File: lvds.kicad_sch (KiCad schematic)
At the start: 19 parts, among them IC10 DS90LV048ATM_NOPB, IC8 DS90LV048ATM_NOPB, IC9 DS90LV048ATM_NOPB

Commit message: Lots of small changes
Some power and ground planes need to be looked at
All parts need to be reexamined before ordering
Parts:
- RLVDS10, RLVDS11, RLVDS2, RLVDS3, RLVDS4, RLVDS5, RLVDS6, RLVDS7, RLVDS8, RLVDS9: Mouser Part Number 71-CRCW0603100RFKEAH -> 667-ERJ-P03F1000V; Mouser Price/Stock https://www.mouser.com/ProductDetail/Vishay-Dale/CRCW060310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 -> https://www.mouser.com/ProductDetail/Panasonic/ERJ-P03F1000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; Power Rating 0.33W -> 0.2W

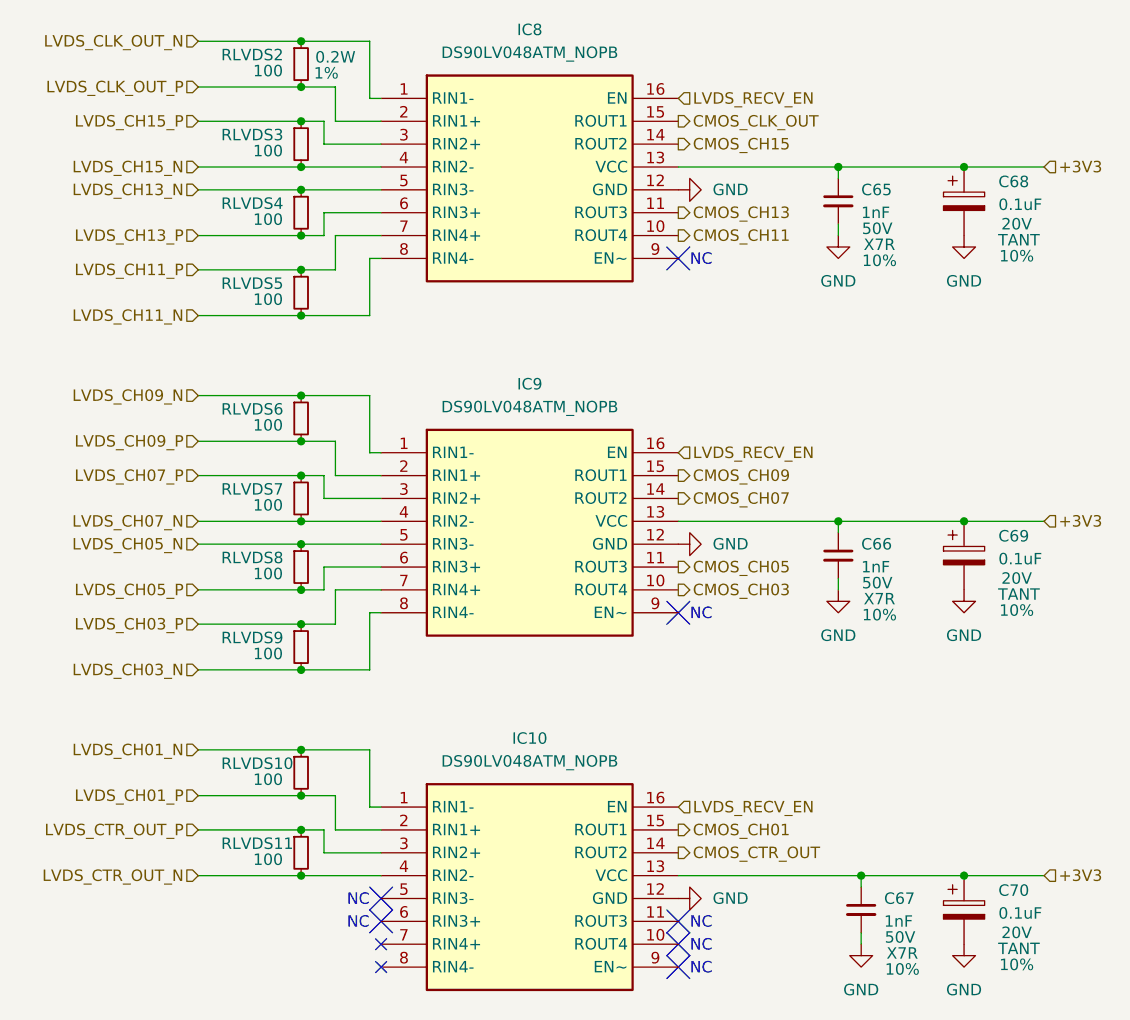
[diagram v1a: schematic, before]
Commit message: Almost done
Taking a break and making a push. Known things to do:
Add pull-up resistors to ETH MDIO, ETH MDC, and XRESL.
Source a 100uF capacitor for primary regulator.
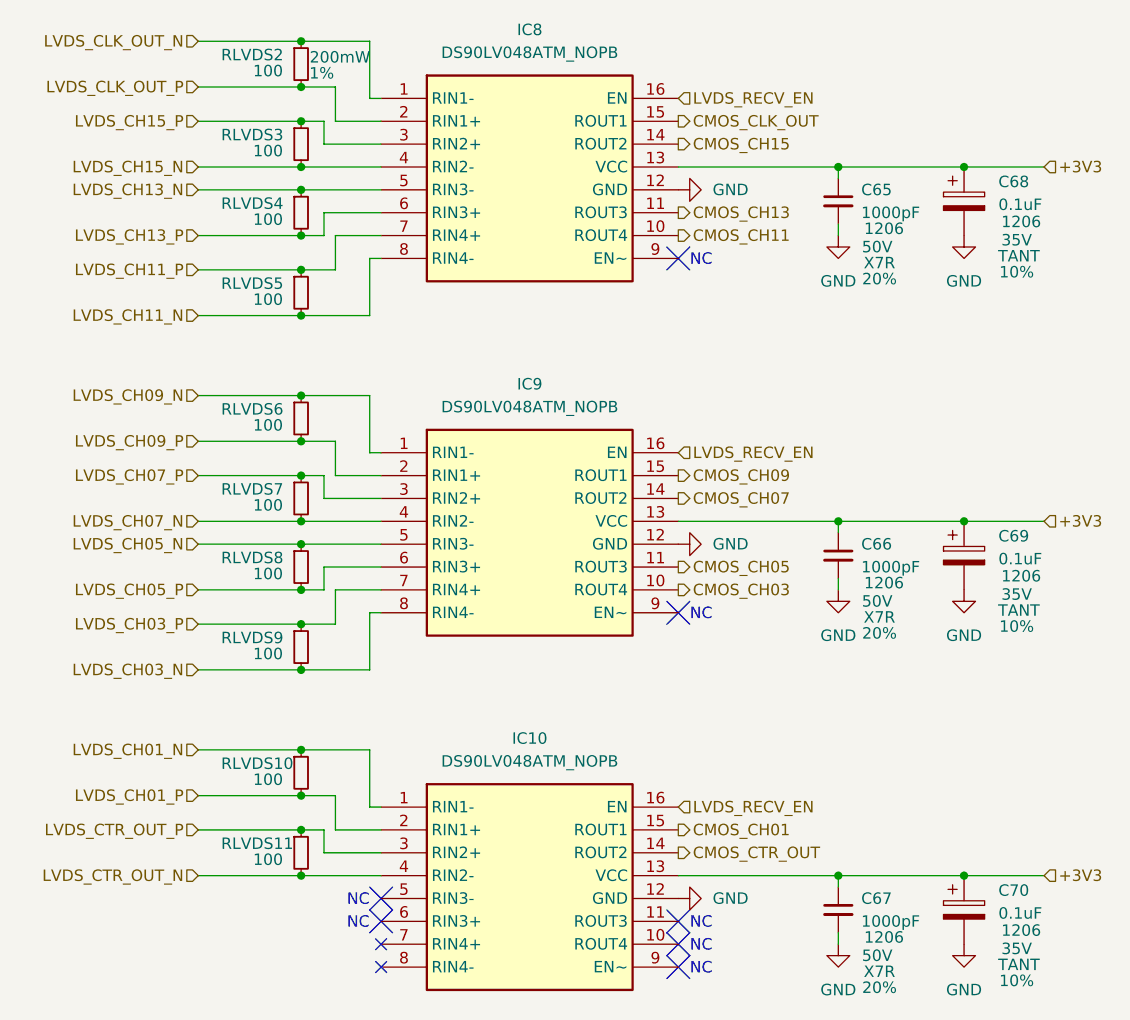
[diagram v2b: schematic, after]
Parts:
- C65, C66, C67: value 1nF -> 1000pF; footprint Capacitor_SMD:C_0603_1608Metric -> Capacitor_SMD:C_1206_3216Metric; Mouser Part Number 581-KAM15AR71H102KM -> 80-C1206C102M5RACTM; Mouser Price/Stock https://www.mouser.com/ProductDetail/KYOCERA-AVX/KAM15AR71H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 -> https://www.mouser.com/ProductDetail/KEMET/C1206C102M5RACTM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; Package Size (none) -> 1206; Tolerance 10% -> 20%
- C68, C69, C70: footprint Capacitor_SMD:C_0805_2012Metric -> Capacitor_SMD:C_1206_3216Metric; Mouser Part Number 581-TAJR104K020R -> 581-TAJA104K035SNJ; Mouser Price/Stock https://www.mouser.com/ProductDetail/KYOCERA-AVX/TAJR104K02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 -> https://www.mouser.com/ProductDetail/KYOCERA-AVX/TAJA104K03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; Package Size (none) -> 1206; Voltage Rating 20V -> 35V
- RLVDS2: Power Rating 0.2W -> 200mW
